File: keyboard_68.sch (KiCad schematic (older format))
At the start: 19 parts, among them J1 Conn_01x02_Male, J70 Conn_02x03_Odd_Even, SW1 EVQPUJ02K / EVQPUA02K, U1 USB_C, U2 nRF52840_som

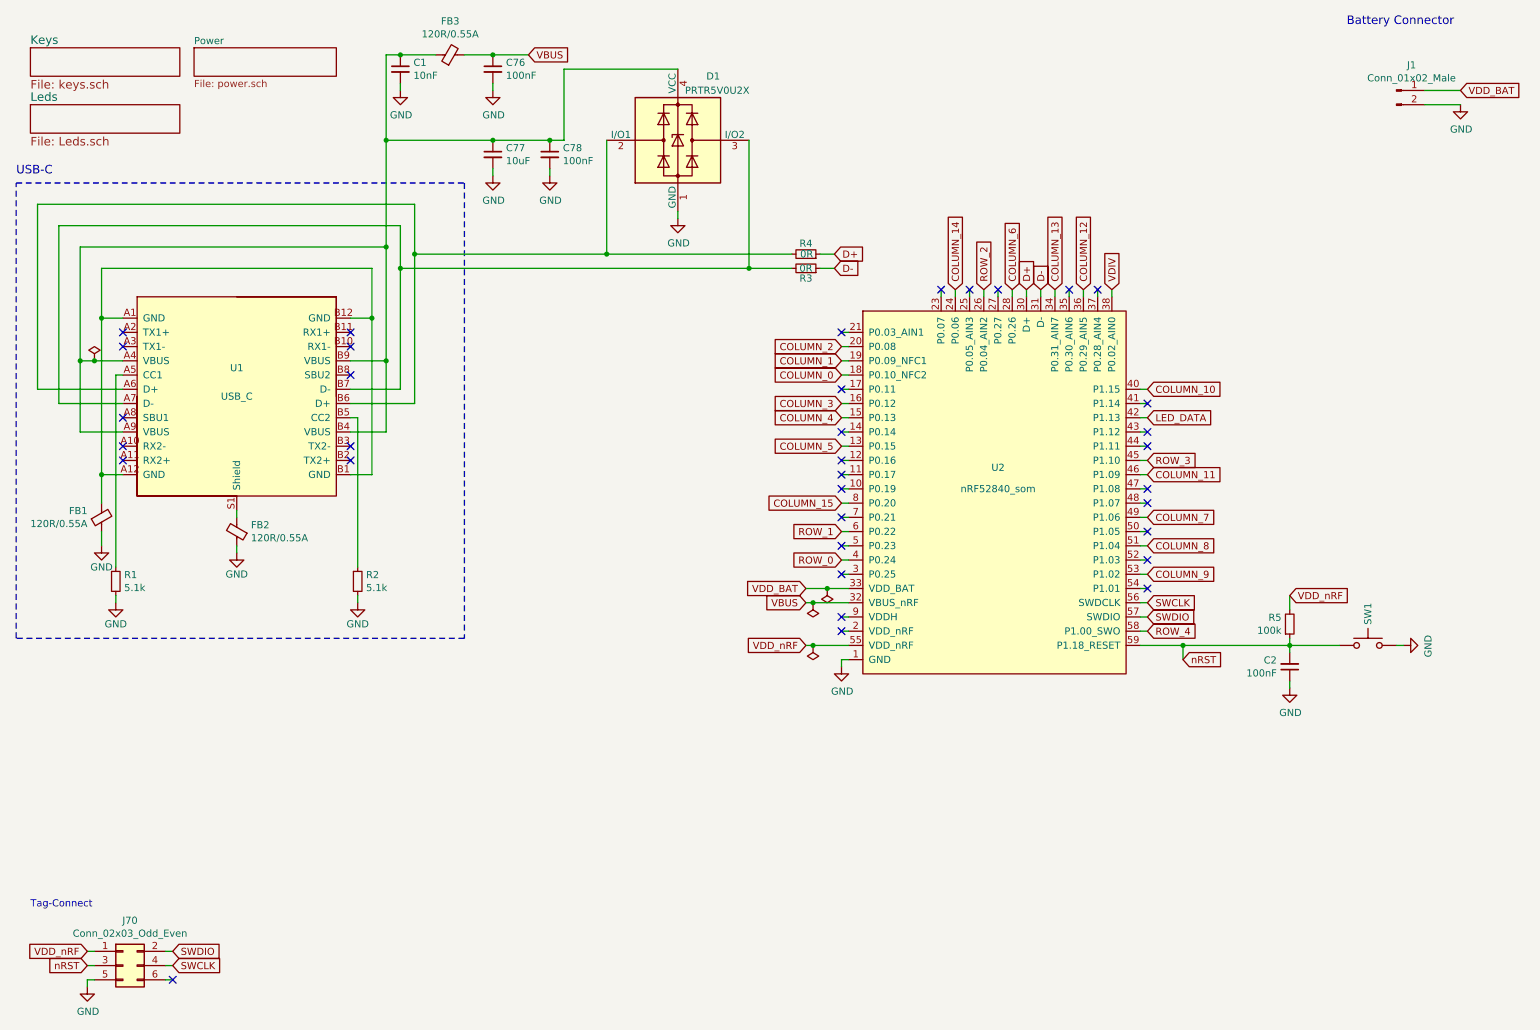
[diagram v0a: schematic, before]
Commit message: add lls, switch and spare gpio connector
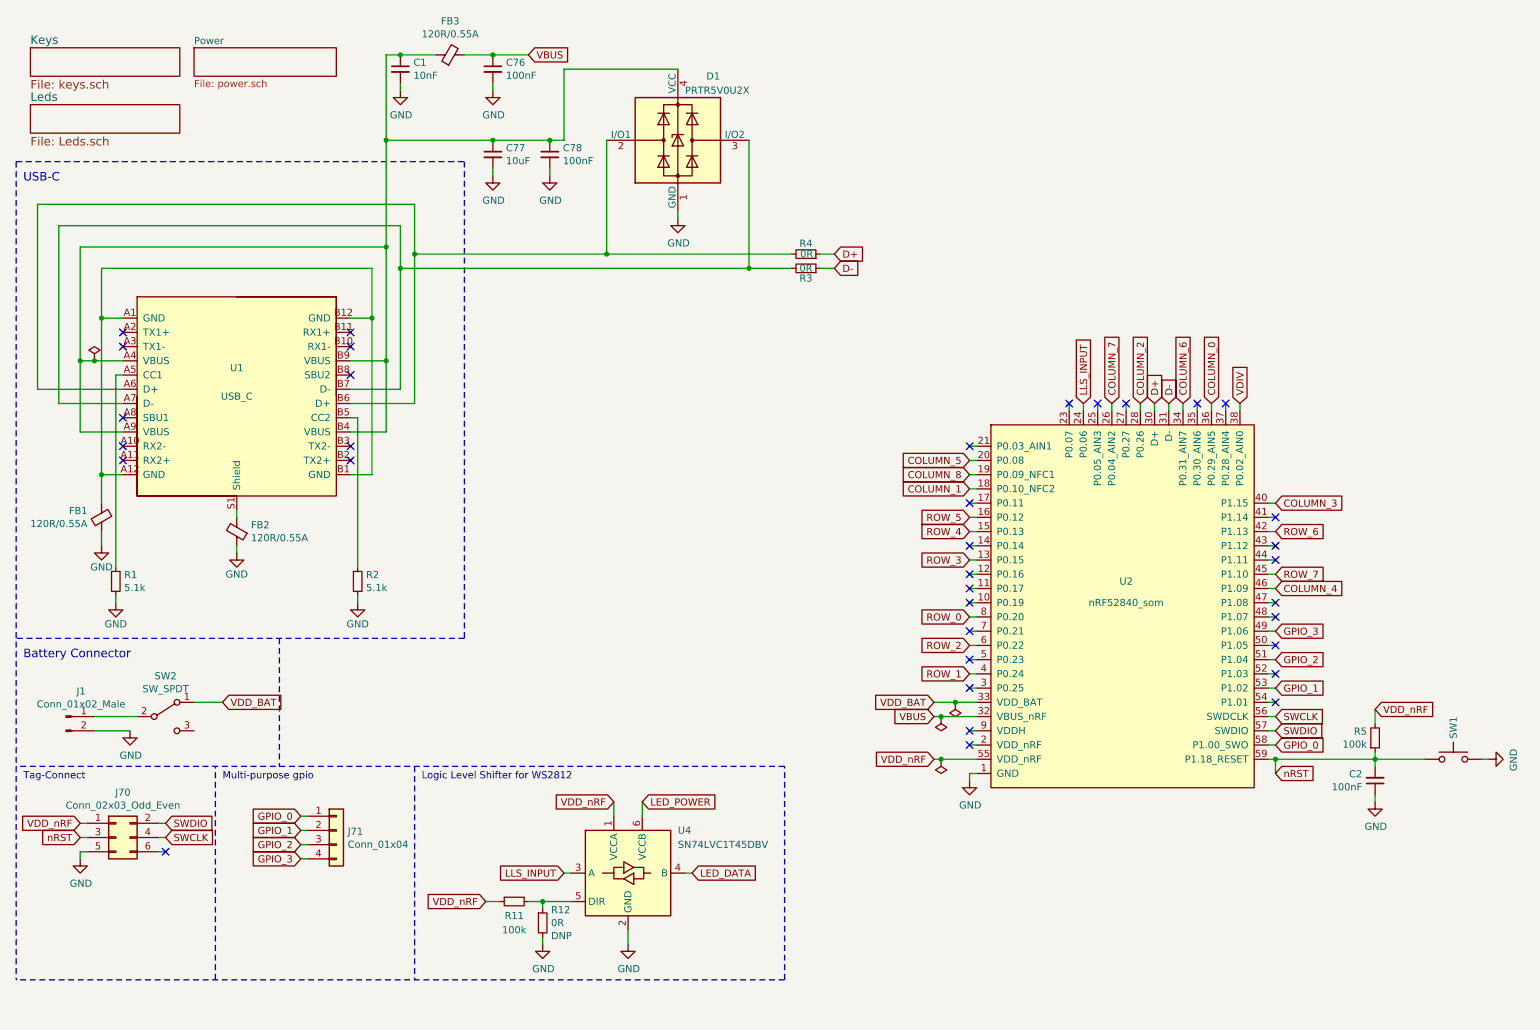
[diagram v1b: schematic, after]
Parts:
- added J71: Conn_01x04, Connector_PinHeader_2.54mm:PinHeader_1x04_P2.54mm_Horizontal, symbol Connector_Generic:Conn_01x04
- added R11: 100k, Resistor_SMD:R_0805_2012Metric, symbol Device:R_Small
- added R12: 0R, Resistor_SMD:R_0805_2012Metric, symbol Device:R_Small
- added SW2: SW_SPDT, custom_footprints:SW_SPDT_CK-JS102011SAQN, symbol Switch:SW_SPDT
- added U4: SN74LVC1T45DBV, Package_TO_SOT_SMD:SOT-23-6, symbol Logic_LevelTranslator:SN74LVC1T45DBV
- J1: Digikey (none) -> 455-1749-1-ND; MPN (none) -> S2B-PH-SM4-TB(LF)(SN); Manufacturer (none) -> JST Sales America Inc.
- J70, U2: DNP (none) -> DNP
- U1: DigiKey 12401610E4#2ACT-ND -> 12401610E4#2ACT-ND; MPN (none) -> 12401610E4#2A; Manufacturer (none) -> Amphenol ICC
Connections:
- net COLUMN_10 is gone; now on net COLUMN_3: U2.40 (P1.15)
- net COLUMN_11 is gone; now on net COLUMN_4: U2.46 (P1.09)
- net COLUMN_12 is gone; now on net COLUMN_0: U2.36 (P0.29_AIN5)
- net COLUMN_13 is gone; now on net COLUMN_6: U2.34 (P0.31_AIN7)
- net COLUMN_15 is gone; now on net ROW_0: U2.8 (P0.20)
- net COLUMN_0: no longer U2.18 (P0.10_NFC2)
- net COLUMN_1: now also U2.18 (P0.10_NFC2); no longer U2.19 (P0.09_NFC1)
- net COLUMN_2: now also U2.28 (P0.26); no longer U2.20 (P0.08)
- net COLUMN_3: no longer U2.16 (P0.12)
- net COLUMN_4: no longer U2.15 (P0.13)
- net COLUMN_5: now also U2.20 (P0.08); no longer U2.13 (P0.15)
- net COLUMN_6: no longer U2.28 (P0.26)
- net COLUMN_7: now also U2.26 (P0.04_AIN2); no longer U2.49 (P1.06)
- net COLUMN_8: now also U2.19 (P0.09_NFC1); no longer U2.51 (P1.04)
- net GND: now also R12.2, U4.2 (GND)
- net LED_DATA: now also U4.4 (B); no longer U2.42 (P1.13)
- net ROW_0: no longer U2.4 (P0.24)
- net ROW_1: now also U2.4 (P0.24); no longer U2.6 (P0.22)
- net ROW_2: now also U2.6 (P0.22); no longer U2.26 (P0.04_AIN2)
- net ROW_3: now also U2.13 (P0.15); no longer U2.45 (P1.10)
- net ROW_4: now also U2.15 (P0.13); no longer U2.58 (P1.00_SWO)
- net VDD_BAT: now also SW2.1 (A); no longer J1.1 (Pin_1)
- net VDD_nRF: now also R11.1, U4.1 (VCCA)
- net COLUMN_14 renamed LLS_INPUT
- net LLS_INPUT: now also U4.3 (A)
- net COLUMN_9 renamed GPIO_1
- net GPIO_1: now also J71.2 (Pin_2)
- new net: J1.1 (Pin_1), SW2.2 (B)
- new net: R11.2, R12.1, U4.5 (DIR)
- new net GPIO_0: J71.1 (Pin_1), U2.58 (P1.00_SWO)
- new net GPIO_2: J71.3 (Pin_3), U2.51 (P1.04)
- new net GPIO_3: J71.4 (Pin_4), U2.49 (P1.06)
- new net LED_POWER: U4.6 (VCCB)
- new net ROW_5: U2.16 (P0.12)
- new net ROW_6: U2.42 (P1.13)
- new net ROW_7: U2.45 (P1.10)
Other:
- note added: "Logic Level Shifter for WS2812"
- note added: "Multi-purpose gpio"
- moved on the sheet: C2, J1, J70, R5, SW1, U2

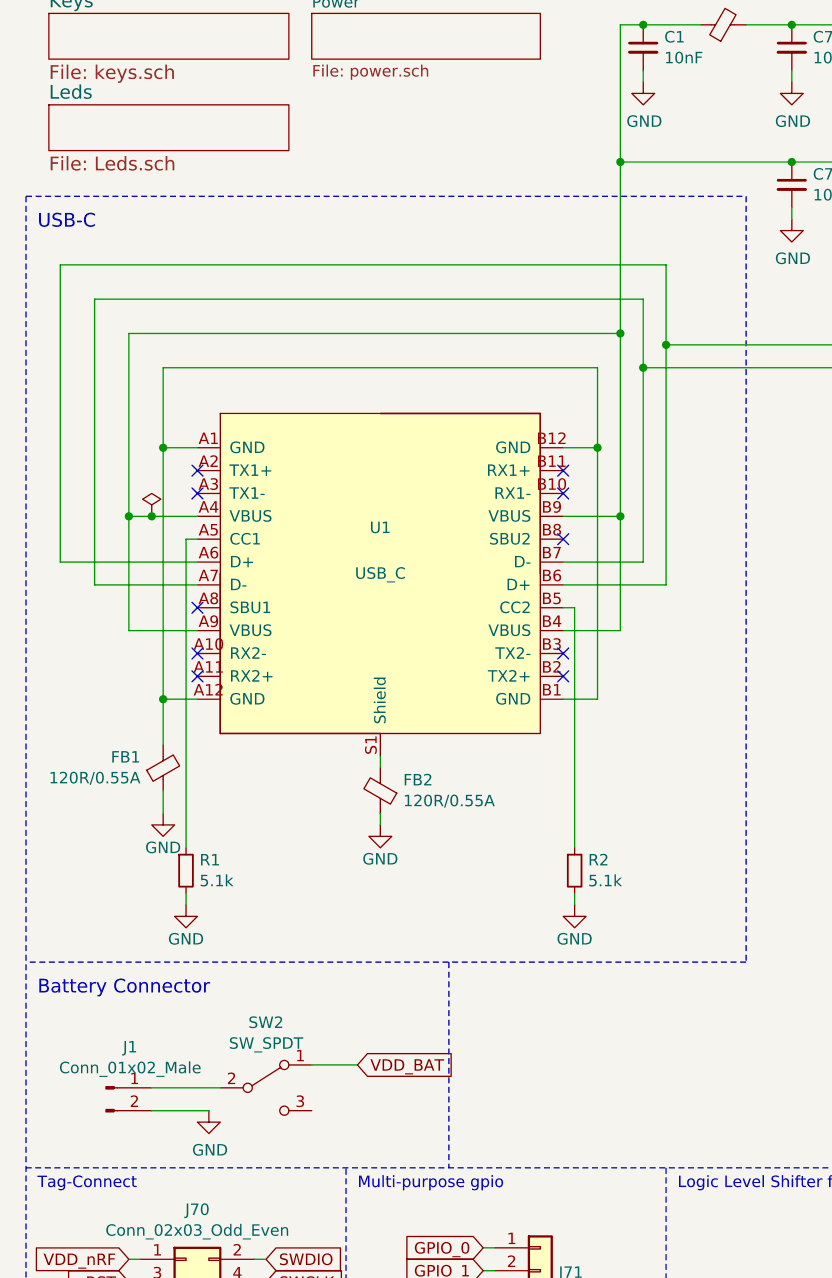
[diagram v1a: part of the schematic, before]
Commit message: change usb c connector, fix column 6
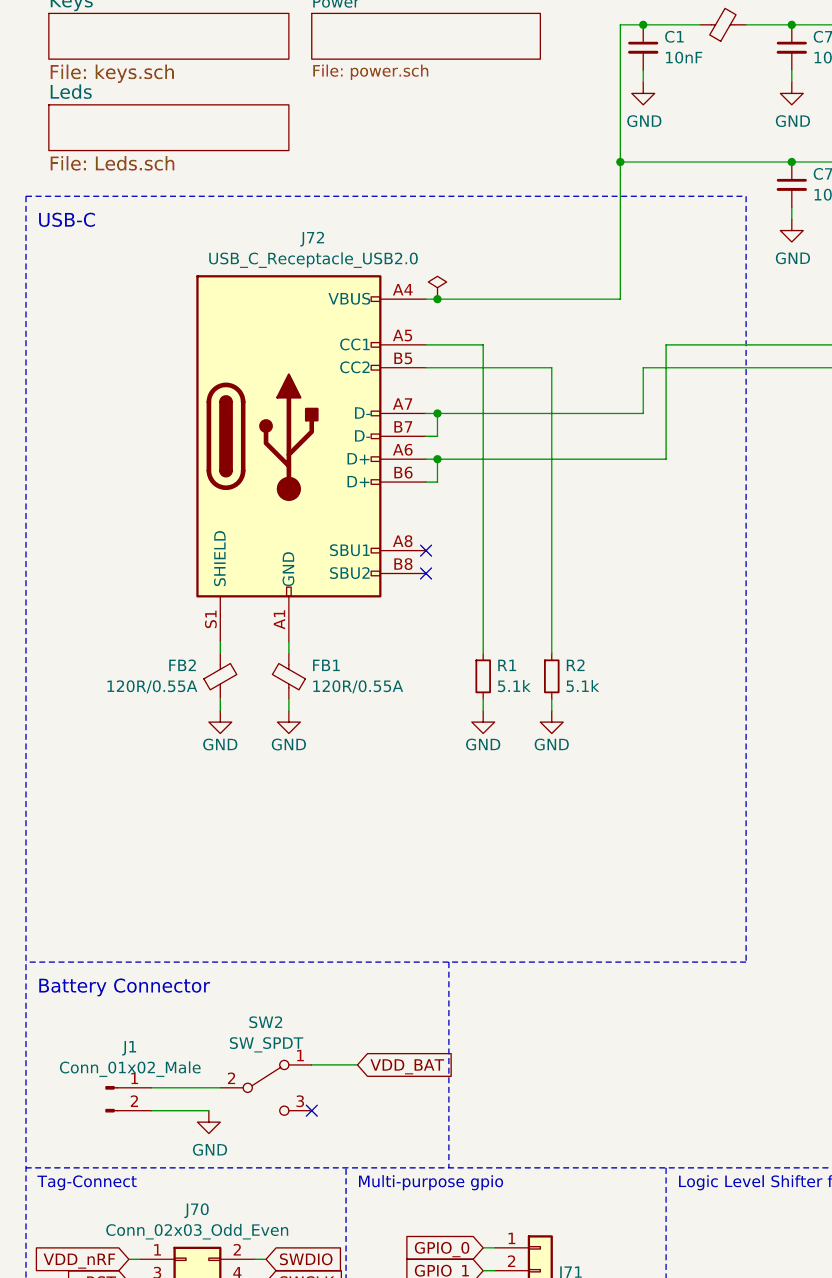
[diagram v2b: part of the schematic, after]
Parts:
- removed U1: USB_C, USB_C_Receptacle_Amphenol_12401610E4-2A:USB_C_Receptacle_Amphenol_12401610E4-2A, symbol usb_type_c:USB_C
- added J72: USB_C_Receptacle_USB2.0, custom_footprints:USB_C_China, symbol Connector:USB_C_Receptacle_USB2.0
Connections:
- net at R1.1: now also J72.A5 (CC1)
- net at R2.1: now also J72.B5 (CC2)
- net at D1.3 (I/O2), R3.2: now also J72.A7 (D-), J72.B7 (D-)
- net at D1.2 (I/O1), R4.2: now also J72.A6 (D+), J72.B6 (D+)
- net at FB1.2: now also J72.A1 (GND), J72.A12 (GND), J72.B1 (GND), J72.B12 (GND)
- net at C1.1, C77.1, C78.1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: now also J72.A4 (VBUS), J72.A9 (VBUS), J72.B4 (VBUS), J72.B9 (VBUS)
- net at FB2.2: now also J72.S1 (SHIELD)
- no-connect marks 35 -> 28
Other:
- moved on the sheet: FB1, FB2, R1, R2

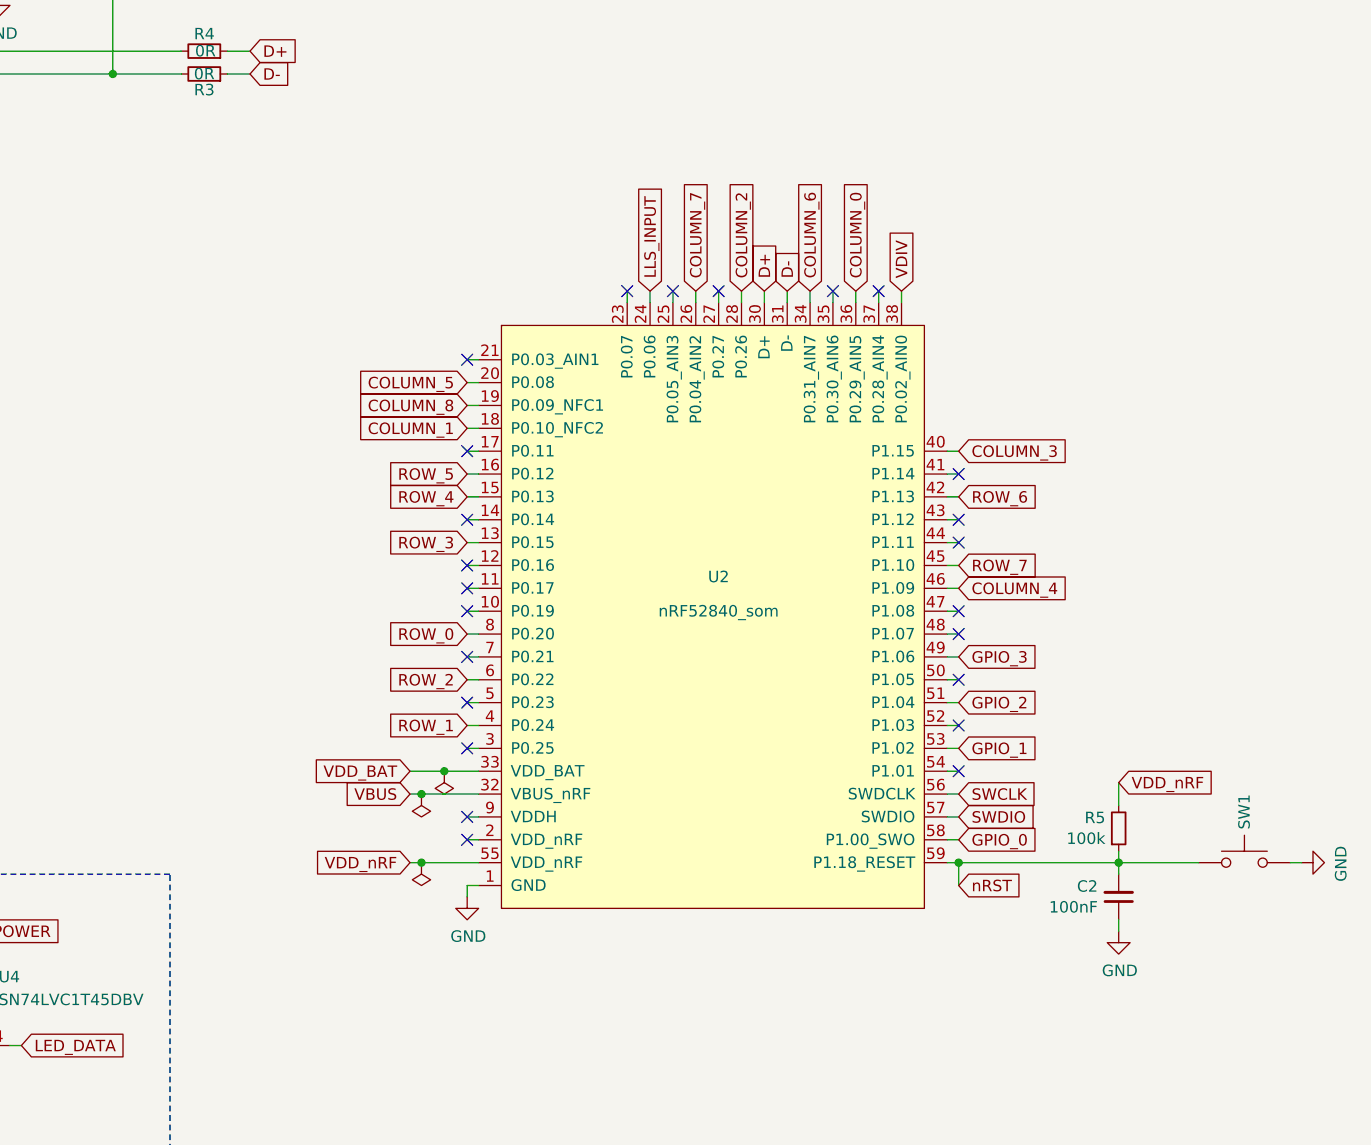
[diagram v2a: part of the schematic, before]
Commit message: switched to smaller module
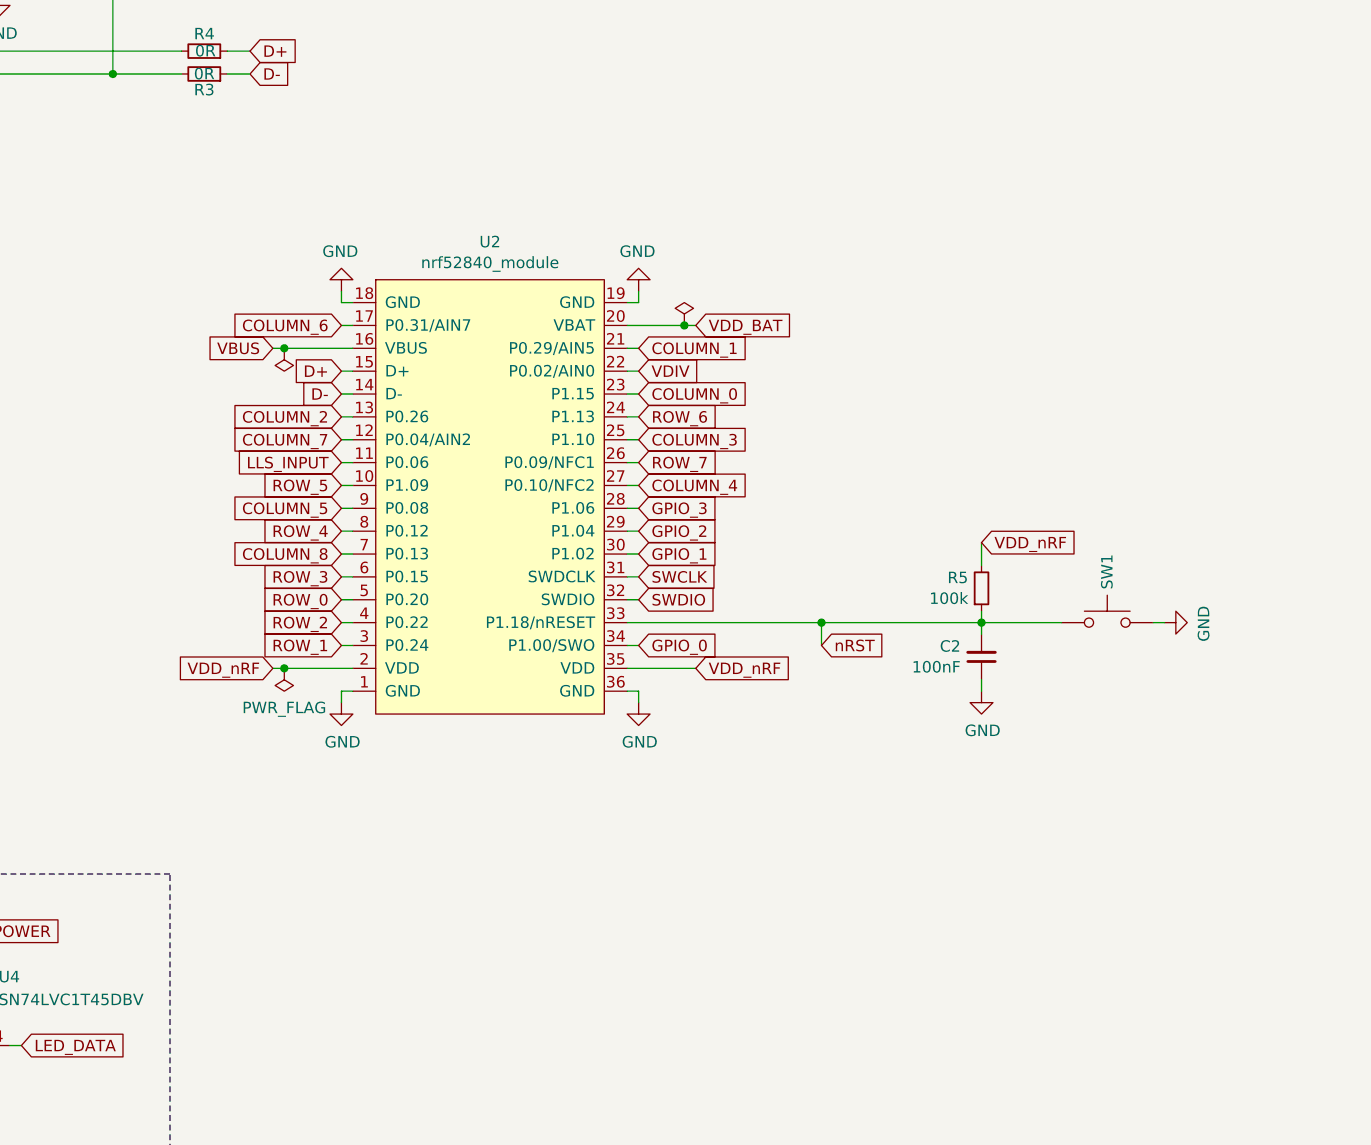
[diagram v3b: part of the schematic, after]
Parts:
- removed U2: nRF52840_som, nrf52840_som:nrf52840_som, symbol nRF52840_som:nRF52840_som
- added U2: nrf52840_module, custom_footprints:nrf52840_module, symbol nRF52840_module:nrf52840_module
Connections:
- net COLUMN_0: now also U2.23 (P1.15)
- net COLUMN_1: now also U2.21 (P0.29/AIN5)
- net COLUMN_2: now also U2.13 (P0.26)
- net COLUMN_3: now also U2.25 (P1.10)
- net COLUMN_4: now also U2.27 (P0.10/NFC2)
- net COLUMN_5: now also U2.9 (P0.08)
- net COLUMN_6: now also U2.17 (P0.31/AIN7)
- net COLUMN_7: now also U2.12 (P0.04/AIN2)
- net COLUMN_8: now also U2.7 (P0.13)
- net D+: now also U2.15 (D+)
- net D-: now also U2.14 (D-)
- net GND: now also U2.1 (GND), U2.18 (GND), U2.19 (GND), U2.36 (GND)
- net GPIO_0: now also U2.34 (P1.00/SWO)
- net GPIO_1: now also U2.30 (P1.02)
- net GPIO_2: now also U2.29 (P1.04)
- net GPIO_3: now also U2.28 (P1.06)
- net LLS_INPUT: now also U2.11 (P0.06)
- net ROW_0: now also U2.5 (P0.20)
- net ROW_1: now also U2.3 (P0.24)
- net ROW_2: now also U2.4 (P0.22)
- net ROW_3: now also U2.6 (P0.15)
- net ROW_4: now also U2.8 (P0.12)
- net ROW_5: now also U2.10 (P1.09)
- net ROW_6: now also U2.24 (P1.13)
- net ROW_7: now also U2.26 (P0.09/NFC1)
- net SWCLK: now also U2.31 (SWDCLK)
- net SWDIO: now also U2.32 (SWDIO)
- net VBUS: now also U2.16 (VBUS)
- net VDD_BAT: now also U2.20 (VBAT)
- net VDD_nRF: now also U2.2 (VDD), U2.35 (VDD)
- net VDIV: now also U2.22 (P0.02/AIN0)
- net nRST: now also U2.33 (P1.18/nRESET)
- no-connect marks 28 -> 4
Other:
- moved on the sheet: C2, R5, SW1
